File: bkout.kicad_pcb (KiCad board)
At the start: 2 copper layers, 20.2 x 11 mm, 11 parts, among them P101 CONN_02X04, U101 SI1102

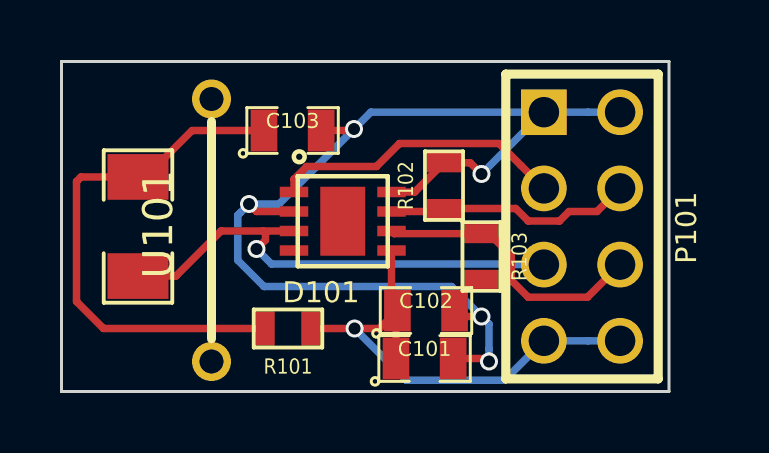
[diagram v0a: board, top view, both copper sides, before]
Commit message: Ajout de serigraphie pour Hugo qui râle :p
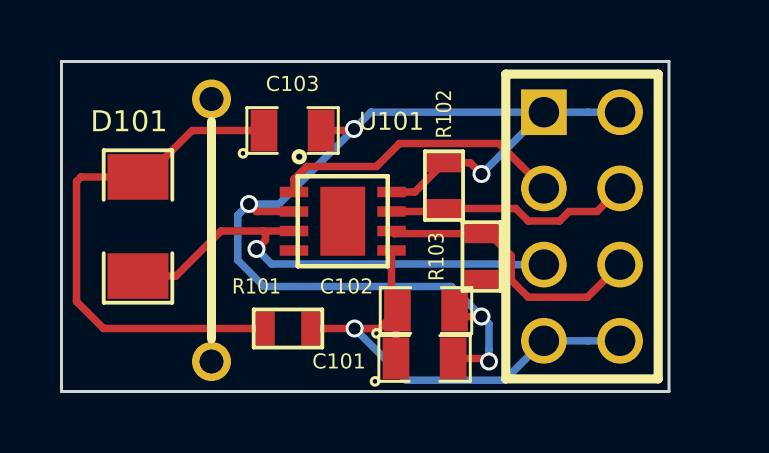
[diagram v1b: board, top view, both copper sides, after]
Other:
- board text added: "FR"
- board text added: "GND"
- board text added: "PRX"
- board text added: "SREN"
- board text added: "TXO"
- board text added: "VCC"
